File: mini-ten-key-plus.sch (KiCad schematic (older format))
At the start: 64 parts, among them SW0 SW_Push, U0 ProMicro

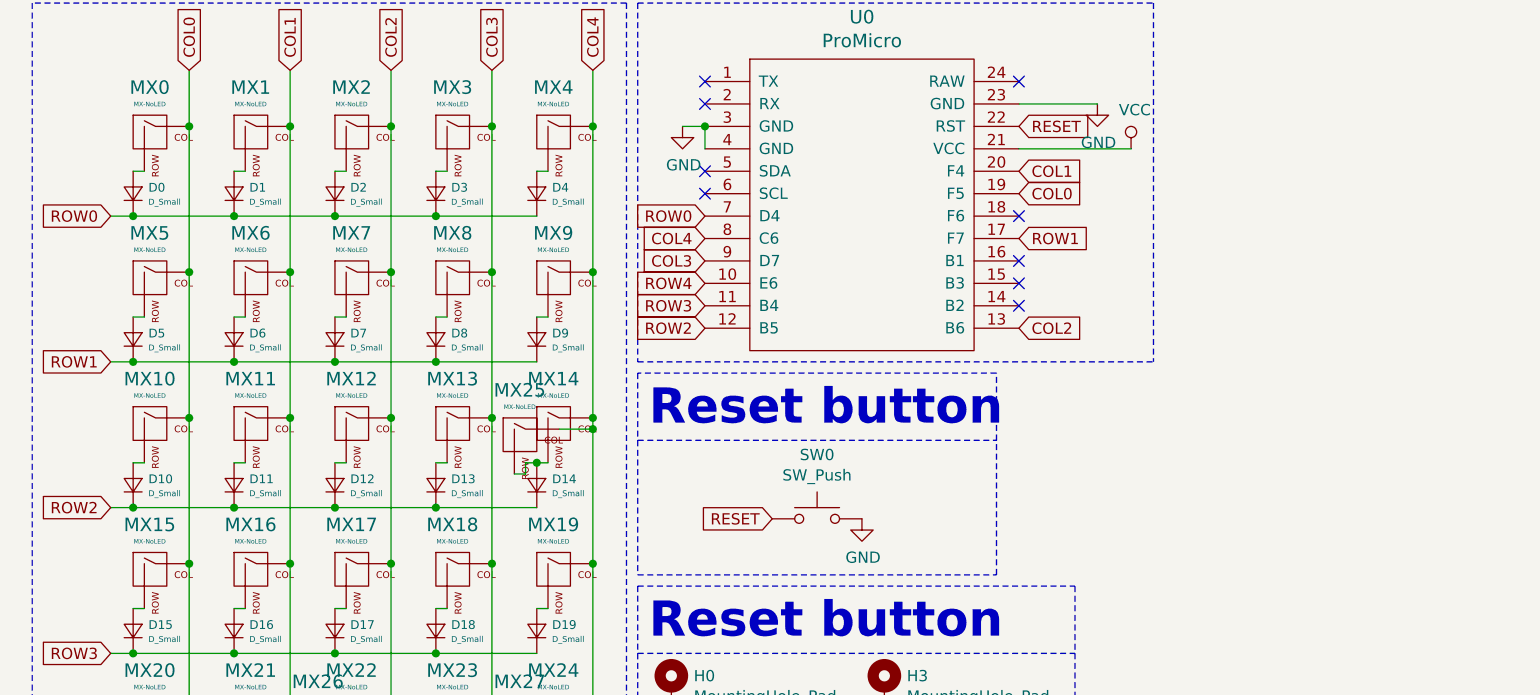
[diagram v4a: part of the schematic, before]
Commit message: Added rotary encoder
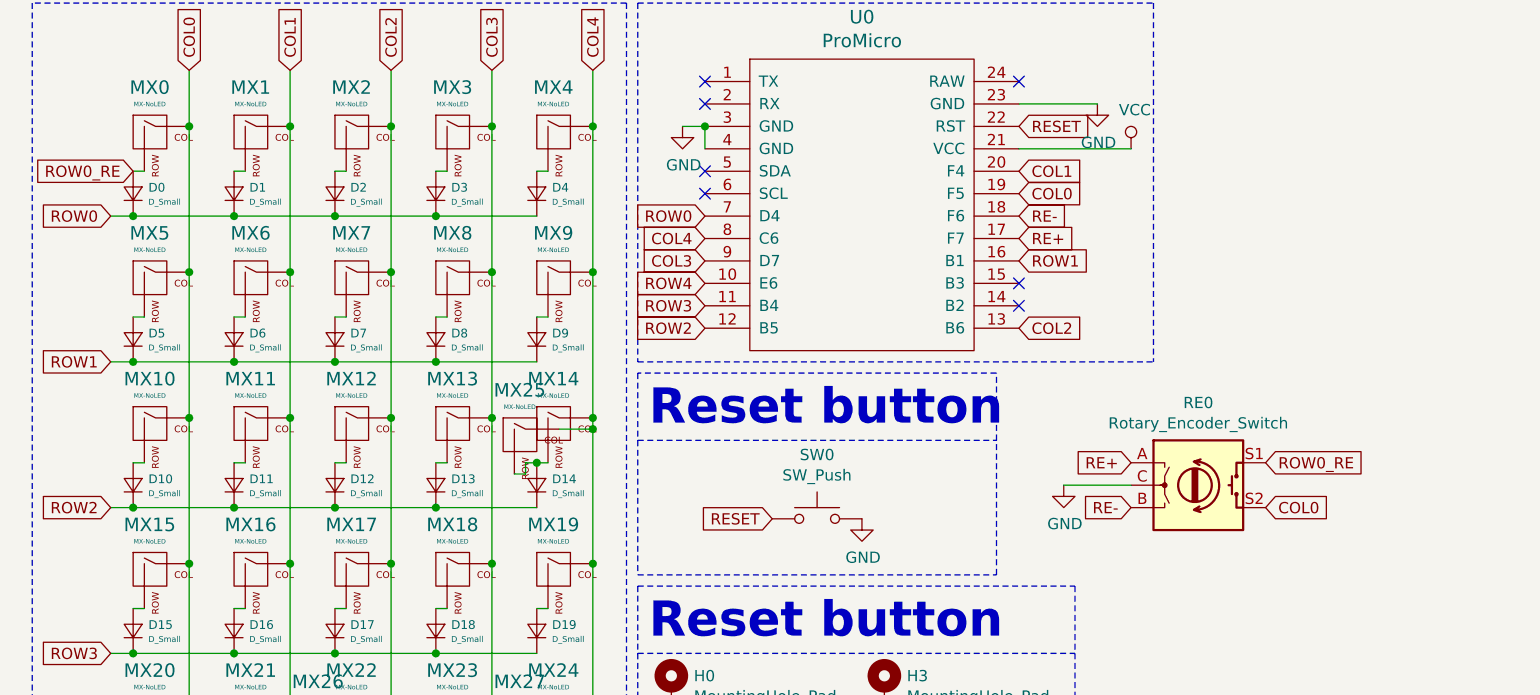
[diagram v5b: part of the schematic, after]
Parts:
- added RE0: Rotary_Encoder_Switch, mini-general-tweaks:RotaryEncoder_Alps_EC11E-Switch-Vertical-EDIT, symbol Device:Rotary_Encoder_Switch
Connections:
- net COL0: now also RE0.S2
- net GND: now also RE0.C
- net ROW1: now also U0.16 (B1); no longer U0.17 (F7)
- net RE-: now reaches U0.18 (F6)
- net RE-: now also RE0.B
- net ROW0_RE: now reaches D0.2 (A), MX0.2 (ROW)
- net ROW0_RE: now also RE0.S1
- new net RE+: RE0.A, U0.17 (F7)
- no-connect marks 9 -> 7
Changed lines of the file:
@@
 Text GLabel 900  3100 0    50   Input ~ 0
 ROW2
-Text GLabel 900  2450 0    50   Input ~ 0
-ROW1
-Text GLabel 900  1800 0    50   Input ~ 0
-ROW0
 Wire Wire Line
 	1000 3100 900  3100
@@
 	1000 4400 1450 4400
 Connection ~ 1000 4400
-Text Notes 600  800  0    157  ~ 31
-Matrix
-Wire Notes Line
-	3200 850  550  850
-Wire Notes Line
-	550  550  3200 550
 Wire Notes Line
 	550  4500 3200 4500
 Wire Notes Line
 	3200 550  3200 4500
-Wire Notes Line
-	550  550  550  4500
 Text Notes 3300 2750 0    157  ~ 31
 Reset button
@@
 COL4
 NoConn ~ 4950 2100
-NoConn ~ 4950 2000
-NoConn ~ 4950 1800
-Text GLabel 4950 1900 2    50   Input ~ 0
+Text GLabel 4950 2000 2    50   Input ~ 0
 ROW1
 NoConn ~ 4950 2200
@@
 	1    0    0    -1
 $EndComp
+$Comp
+L Device:Rotary_Encoder_Switch RE0
+U 1 1 61846C32
+P 5750 3000
+F 0 "RE0" H 5750 3367 50  0000 C CNN
+F 1 "Rotary_Encoder_Switch" H 5750 3276 50  0000 C CNN
+F 2 "mini-general-tweaks:RotaryEncoder_Alps_EC11E-Switch-Vertical-EDIT" H 5600 3160 50  0001 C CNN
+F 3 "~" H 5750 3260 50  0001 C CNN
+	1    5750 3000
+	1    0    0    -1
+$EndComp
+Wire Notes Line
+	550  550  550  4500
+Wire Notes Line
+	550  550  3200 550
+Wire Notes Line
+	3200 850  550  850
+Text Notes 600  800  0    157  ~ 31
+Matrix
+Text GLabel 900  1800 0    50   Input ~ 0
+ROW0
+Text GLabel 900  2450 0    50   Input ~ 0
+ROW1
+Text GLabel 6050 3100 2    50   Input ~ 0
+COL0
+$Comp
+L power:GND #PWR0101
+U 1 1 618707FF
+P 5150 3000
+F 0 "#PWR0101" H 5150 2750 50  0001 C CNN
+F 1 "GND" H 5155 2827 50  0000 C CNN
+F 2 "" H 5150 3000 50  0001 C CNN
+F 3 "" H 5150 3000 50  0001 C CNN
+	1    5150 3000
+	1    0    0    -1
+$EndComp
+Wire Wire Line
+	5150 3000 5450 3000
+Text GLabel 6050 2900 2    50   Input ~ 0
+ROW0_RE
+Text GLabel 1000 1600 0    50   Input ~ 0
+ROW0_RE
+Text GLabel 4950 1900 2    50   Input ~ 0
+RE+
+Text GLabel 5450 3100 0    50   Input ~ 0
+RE-
+Text GLabel 5450 2900 0    50   Input ~ 0
+RE+
+Text GLabel 4950 1800 2    50   Input ~ 0
+RE-
 $EndSCHEMATC

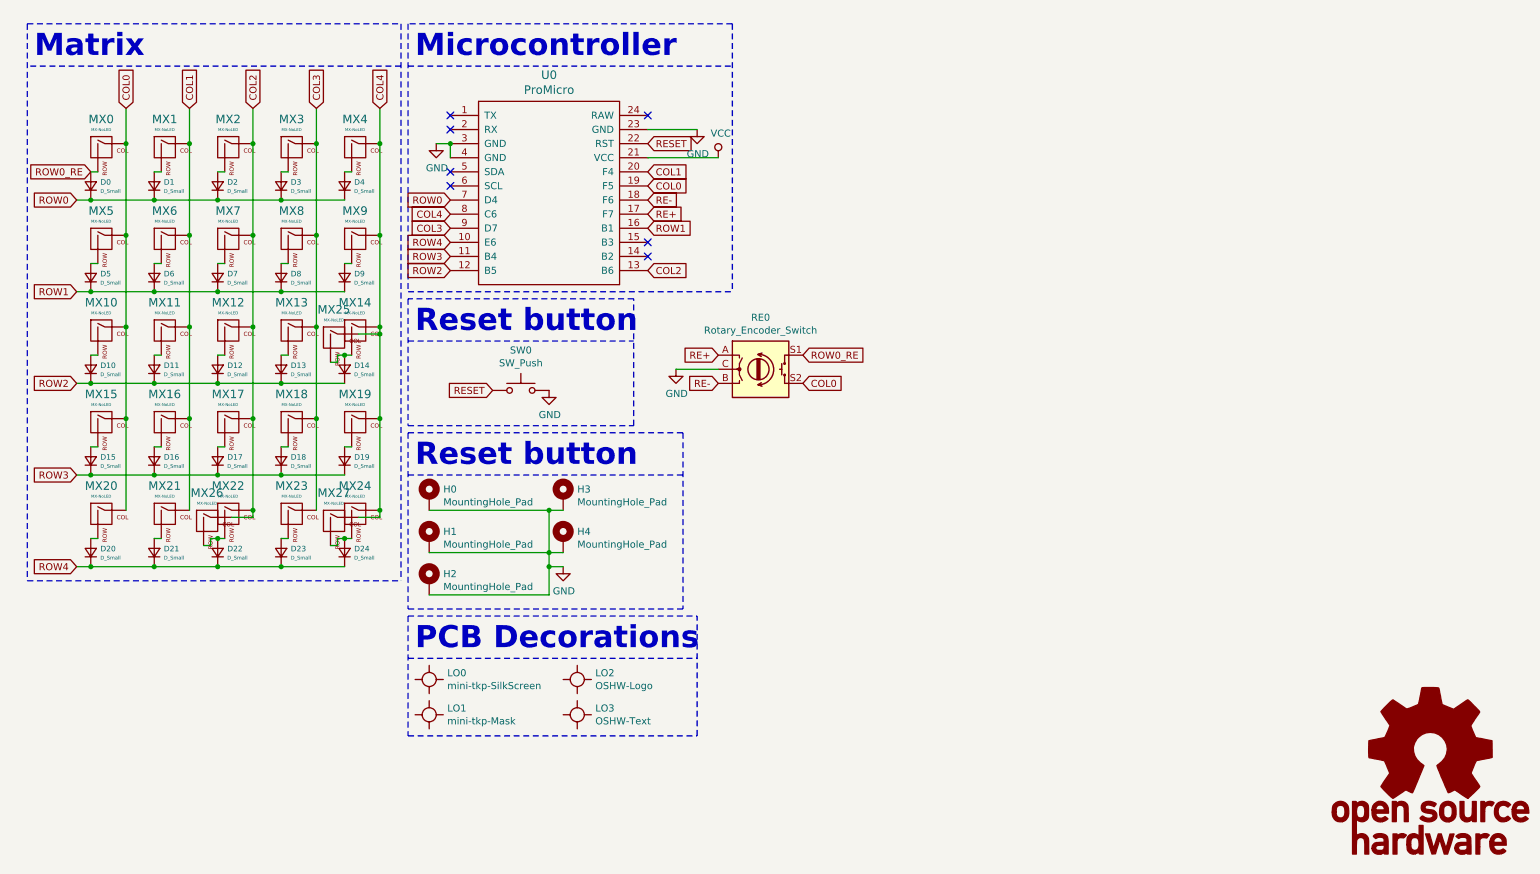
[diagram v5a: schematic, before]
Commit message: Added TKP logo, restructured schematic
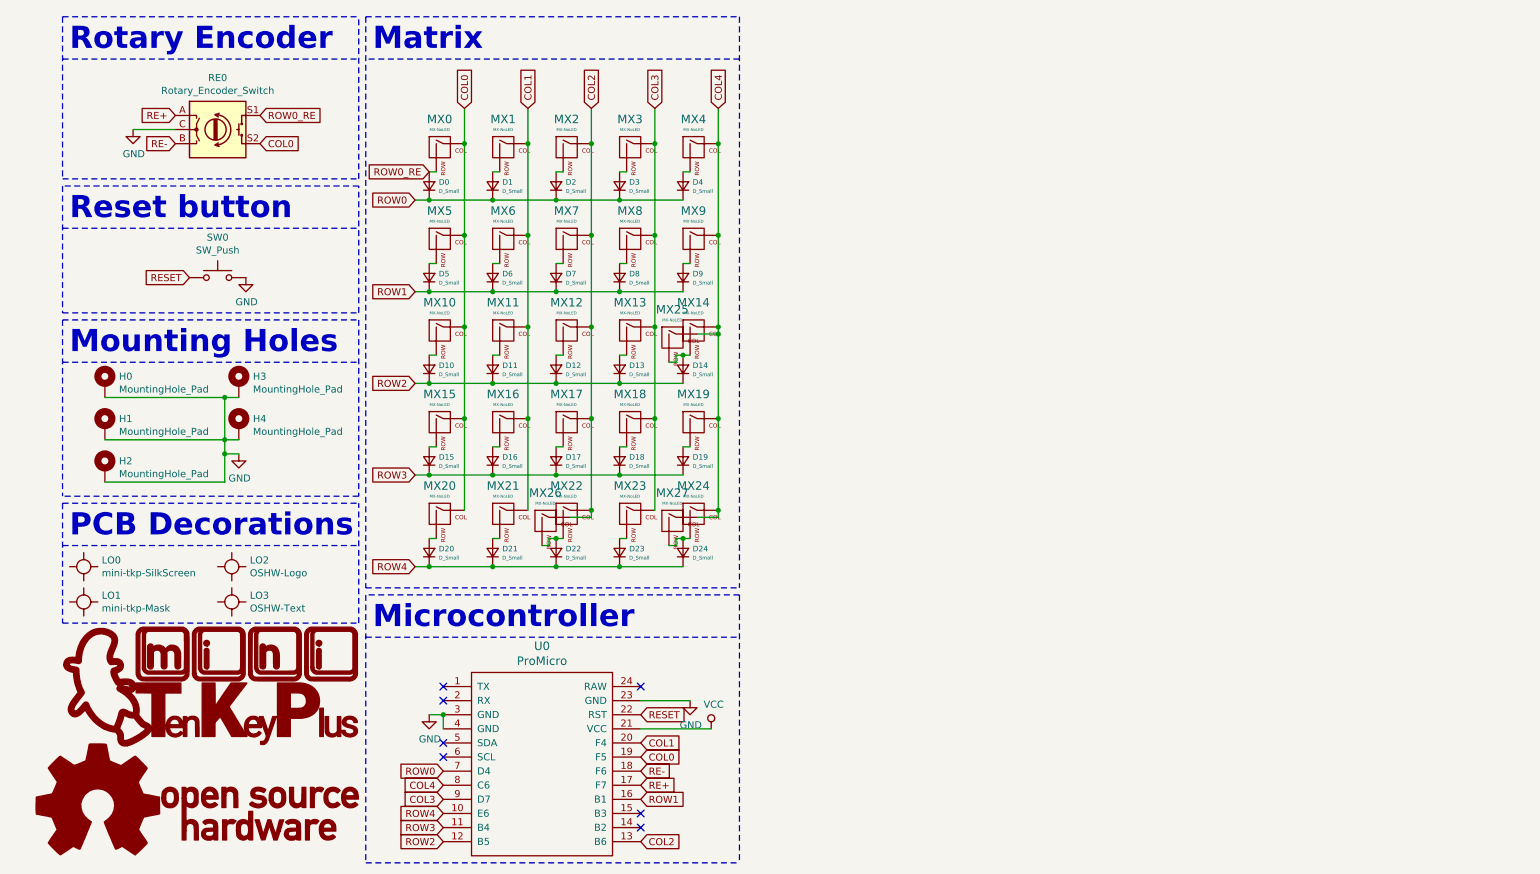
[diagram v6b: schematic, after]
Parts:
- LO0: footprint mini-Logos:eLiXiVy-rev1.1-SilkScreen -> mini-Logos:mini-TKP-BSilk
- LO1: footprint mini-Logos:eLiXiVy-rev1.1-Mask -> mini-Logos:mini-TKP-BMask
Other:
- note added: "Mounting Holes"
- note added: "Rotary Encoder"
- moved on the sheet: D0, D1, D10, D11, D12, D13, D14, D15, D16, D17, D18, D19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

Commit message: Added layout image and general edits
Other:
- moved on the sheet: D0, D1, D10, D11, D12, D13, D14, D15, D16, D17, D18, D19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

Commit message: Added LICENSE
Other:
- moved on the sheet: D0, D1, D10, D11, D12, D13, D14, D15, D16, D17, D18, D19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
